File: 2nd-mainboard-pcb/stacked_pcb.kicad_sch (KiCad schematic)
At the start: 16 parts, among them J12 Steckverbinder_Male_Fans, J13 Steckverbinder_Female_Leistung, J14 Steckverbinder_Male_Leistung, J15 Steckverbinder_Female_Motoren

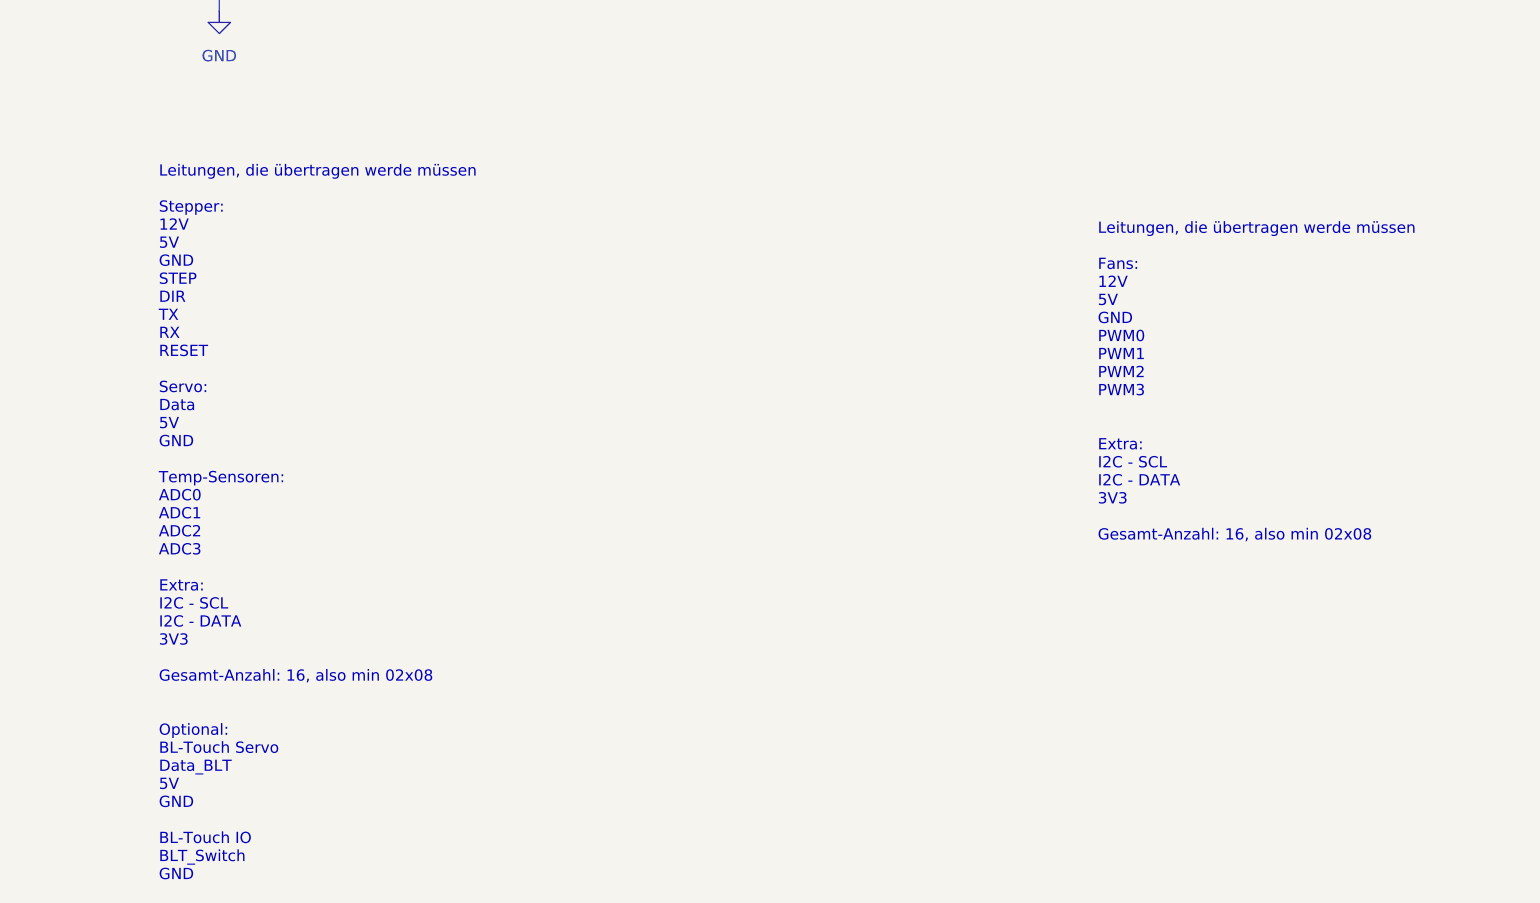
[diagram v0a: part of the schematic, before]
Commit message: updated a bit of the track widths, removed comments in schematic
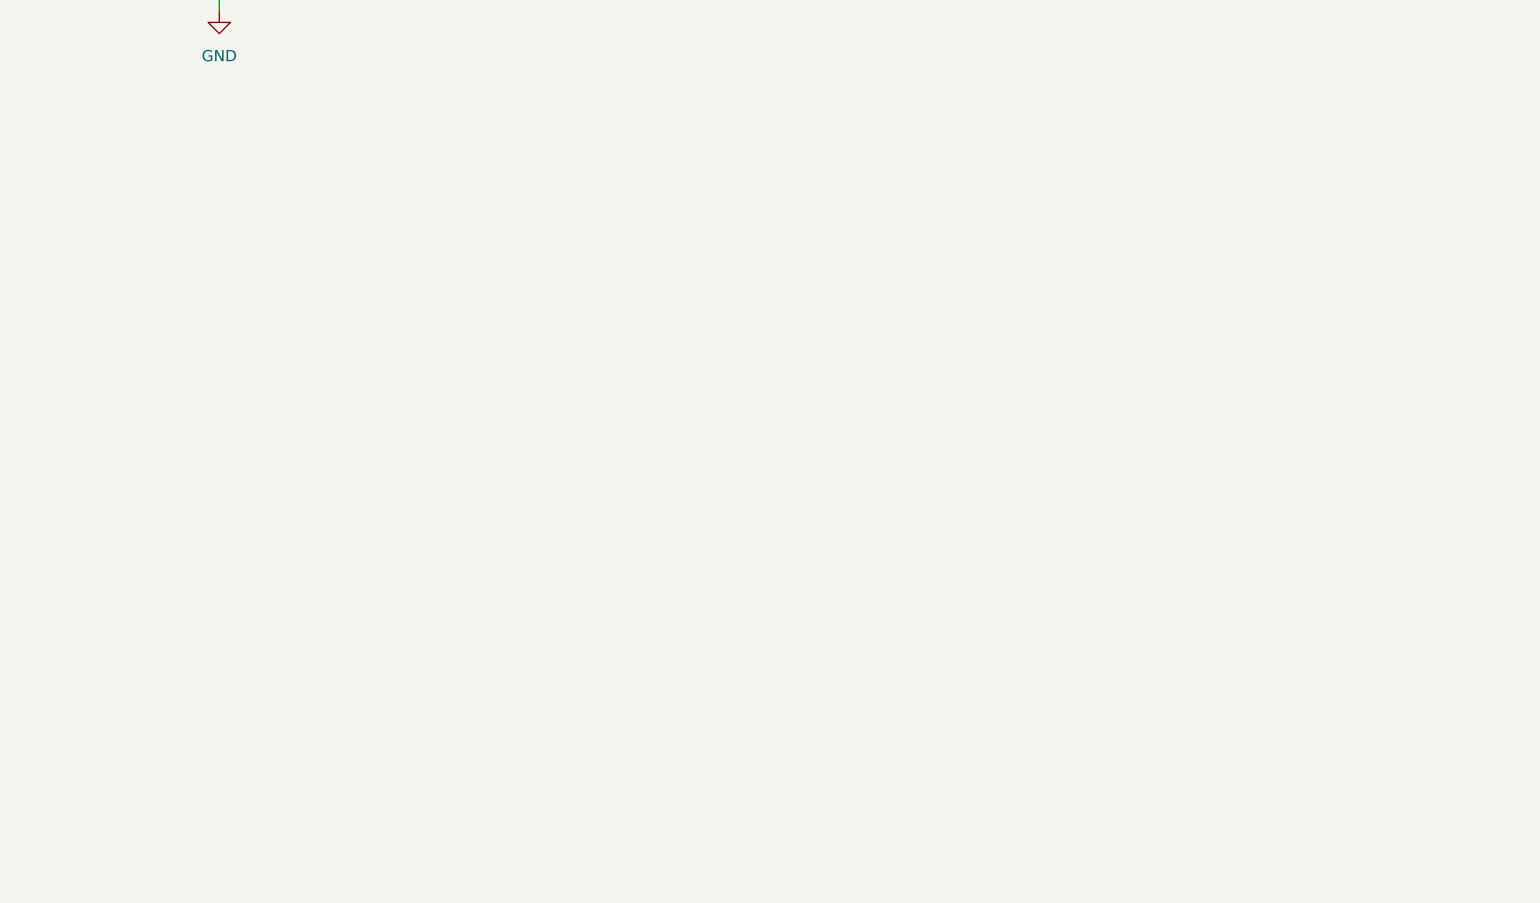
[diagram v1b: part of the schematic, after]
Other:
- note removed: "Leitungen, die übertragen werde müssen Fans: 12V 5V GND PWM0 PWM1 PWM2 PWM3 Extra: I2C - SCL I2C - DATA 3V3 Gesamt-Anzahl: 16, also min 02x08"
- note removed: "Leitungen, die übertragen werde müssen Stepper: 12V 5V GND STEP DIR TX RX RESET Servo: Data 5V GND Temp-Sensoren: ADC0 ADC1 ADC2 ADC3 Extra: I2C - SCL I2C - DATA 3V3 Gesamt-Anzahl: 16, also min 02x08 Optional: BL-Touch Servo Data_BLT 5V GND BL-Touch IO BLT_Switch GND"
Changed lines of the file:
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@@
-		)
-	)
-	(text "Leitungen, die übertragen werde müssen\n\nFans:\n12V\n5V\nGND\nPWM0\nPWM1\nPWM2\nPWM3\n\n\nExtra:\nI2C - SCL\nI2C - DATA\n3V3\n\nGesamt-Anzahl: 16, also min 02x08\n"
-		(exclude_from_sim no)
-		(at 237.998 131.064 0)
-		(effects
-			(font
-				(size 1.27 1.27)
-			)
-			(justify left)
 		)
 	)
@@
 		)
 	)
-	(text "Leitungen, die übertragen werde müssen\n\nStepper:\n12V\n5V\nGND\nSTEP\nDIR\nTX\nRX\nRESET\n\nServo:\nData\n5V\nGND\n\nTemp-Sensoren:\nADC0\nADC1\nADC2\nADC3\n\nExtra:\nI2C - SCL\nI2C - DATA\n3V3\n\nGesamt-Anzahl: 16, also min 02x08\n\n\nOptional:\nBL-Touch Servo\nData_BLT\n5V\nGND\n\nBL-Touch IO\nBLT_Switch\nGND\n"
-		(exclude_from_sim no)
-		(at 131.572 147.066 0)
-		(effects
-			(font
-				(size 1.27 1.27)
-			)
-			(justify left)
-		)
-	)

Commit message: cad files gebastelt
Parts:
- removed J14: Steckverbinder_Male_Leistung, Imported_Component_Footprints:SAMTEC_TSM-107-04-L-DV, symbol Imported_Component_Symbols:TSM-107-04-L-DV
- added J24: Steckverbinder_Male_Leistung, Imported_Component_Footprints:SAMTEC_HW-07-08-L-D-250-SM, symbol Imported_Component_Symbols:HW-07-08-L-D-250-SM
- H1, H2, H3, H4: footprint MountingHole:MountingHole_2.2mm_M2_Pad_TopBottom -> Imported_Component_Footprints:MountingHole_2.7mm_M2.5_ISO7380_Pad_TopBottom_7mm
- H10, H11, H12, H9: footprint MountingHole:MountingHole_2.2mm_M2_Pad_TopBottom -> MountingHole:MountingHole_2.7mm_M2.5_ISO7380_Pad_TopBottom
- H5, H6, H7, H8: footprint MountingHole:MountingHole_2.2mm_M2_Pad_TopBottom -> Imported_Component_Footprints:MountingHole_2.7mm_M2.5_ISO7380_Pad_TopBottom_111mm
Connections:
- net +12V: now also J24.03
- net +5V_POW: now also J24.05
- net BLT_Servo: now also J24.10
- net BLT_Switch: now also J24.12
- net DIR: now also J24.08
- net GND: now also J24.01
- net LED_3: now also J24.11
- net RXD: now also J24.04
- net SCL: now also J24.14
- net SDA: now also J24.02
- net SM_Servo: now also J24.09
- net STEP: now also J24.07
- net TXD: now also J24.06

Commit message: stacked pcb reworked
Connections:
- net RXD is gone; now on net +5V_USBC: J15.04, J24.04
- net +5V_USBC: now also J12.02; no longer J12.07
- net ADC0: now also J12.06; no longer J12.08
- net ADC1: now also J12.08; no longer J12.10
- net ADC2: now also J12.10; no longer J12.12
- net ADC3: now also J12.12; no longer J12.14
- net FAN_01_PWM_clockwise: now also J12.07; no longer J12.04
- net FAN_01_PWM_counterclockwise: now also J12.09; no longer J12.02
- net LED_MOT0: now reaches J24.13
- net LED_MOT0: now also J15.13
- net LED_2 renamed LED_FAN1
- net LED_FAN1: now also J12.04; no longer J12.09
- net LED_3 renamed LED_MOT1
- net SMD_TEMP_0 renamed LED_FAN0
- net LED_FAN0: now also J12.14; no longer J12.06
- net TXD renamed RESET
- no-connect marks 2 -> 0
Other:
- note removed: "Modul 1: Fans"
- note removed: "Modul 2: Atmega + Leistungs-Eingänge"
- note removed: "Modul 3: Motoren"
- note removed: "Mounting Holes für Montage der Platine"
- moved on the sheet: H1, H10, H11, H12, H2, H3, H4, H5, H6, H7, H8, H9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
